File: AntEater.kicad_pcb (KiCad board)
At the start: 4 copper layers, 49.8 x 48.6 mm, 39 parts, among them CN1 X2026WRS-2X09D-LPSW, CN2 X2026WRS-2X09D-LPSW, J2 USB_C_Receptacle_USB2.0, J3 Conn_02x06_Odd_Even, U1 M93C46-WDW6TP, U2 FT4232HQ, U3 RT9080-33GJ5, Y1 12MHz

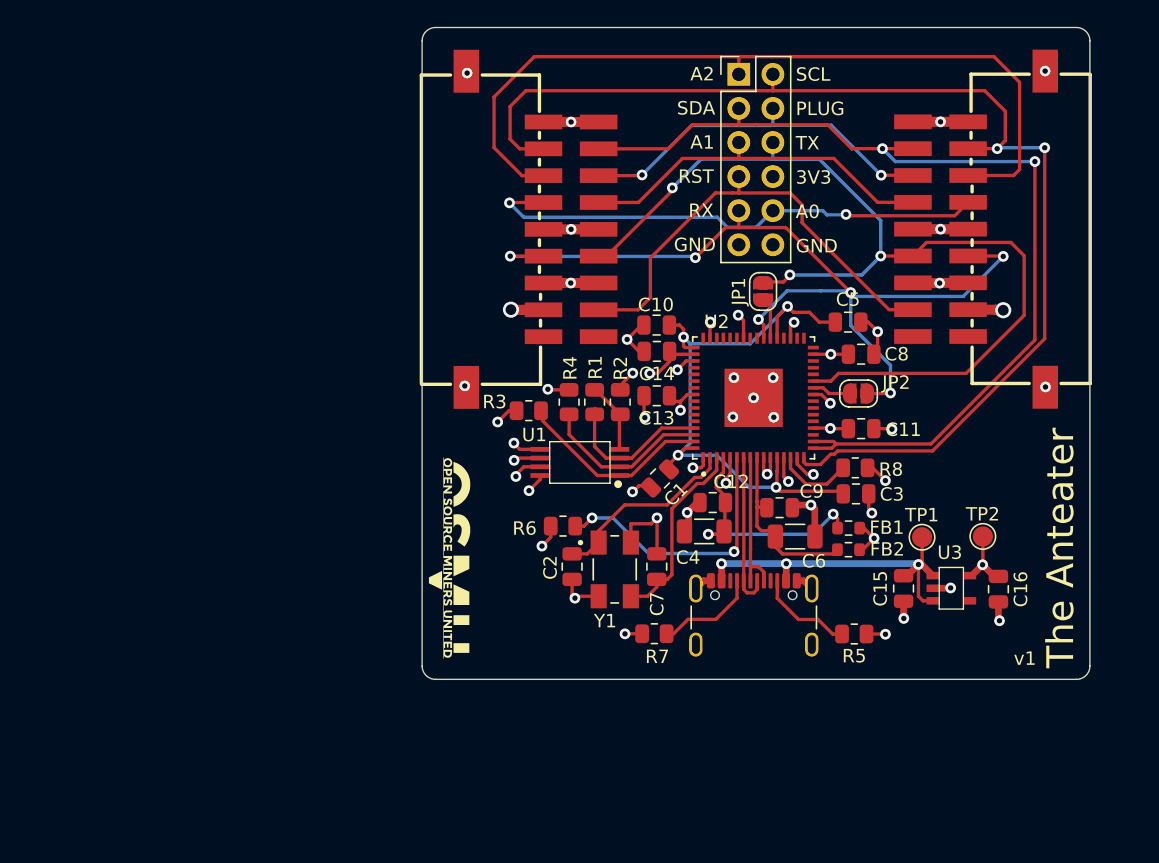
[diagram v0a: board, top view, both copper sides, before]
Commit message: switched schematic to RP2040
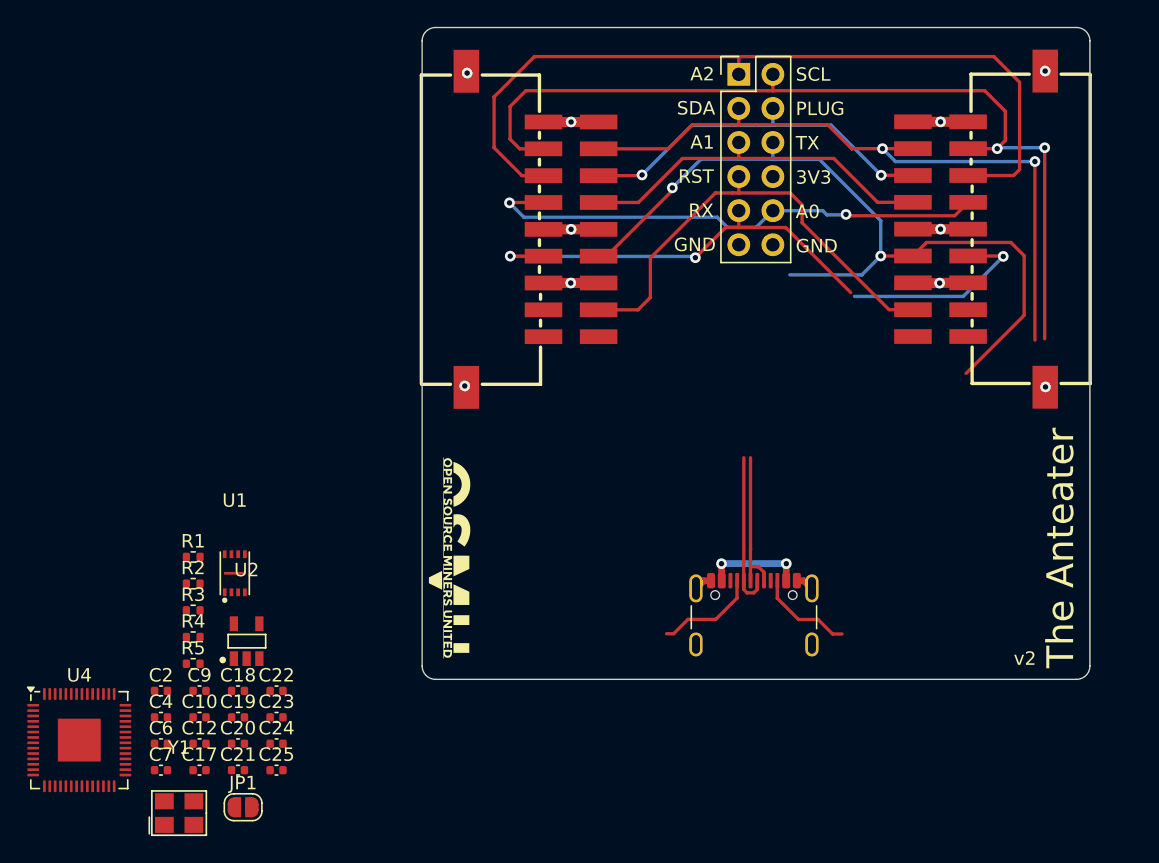
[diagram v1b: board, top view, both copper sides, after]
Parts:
- removed C1, C11, C13, C14, C3, C5, C8: 0.1uF, Capacitor_SMD:C_0805_2012Metric
- removed C15, C16: 1uF, Capacitor_SMD:C_0805_2012Metric
- removed FB1, FB2: FerriteBead_Small, Resistor_SMD:R_0603_1608Metric
- removed J2: USB_C_Receptacle_USB2.0, antsniffer:USB_C_Receptacle_GCT_USB4105-xx-A_16P_TopMnt_Horizontal
- removed JP2: SolderJumper_2_Open, Jumper:SolderJumper-2_P1.3mm_Open_RoundedPad1.0x1.5mm
- removed R6: 12K, Resistor_SMD:R_0805_2012Metric
- removed R7: 5.1K, Resistor_SMD:R_0805_2012Metric
- removed R8: 1K, Resistor_SMD:R_0805_2012Metric
- removed TP1, TP2: TestPoint, TestPoint:TestPoint_Pad_D1.5mm
- removed U3: RT9080-33GJ5, antsniffer:RT9080-33GJ5
- added C17: 1uF, Capacitor_SMD:C_0402_1005Metric, F.Cu at (98.7, 127.7)
- added C18: 1uF, Capacitor_SMD:C_0402_1005Metric, F.Cu at (101.5, 121.8)
- added C19: 0.1uF, Capacitor_SMD:C_0402_1005Metric, F.Cu at (101.5, 123.8)
- added C20: 0.1uF, Capacitor_SMD:C_0402_1005Metric, F.Cu at (101.5, 125.8)
- added C21: 0.1uF, Capacitor_SMD:C_0402_1005Metric, F.Cu at (101.5, 127.7)
- added C22: 0.1uF, Capacitor_SMD:C_0402_1005Metric, F.Cu at (104.4, 121.8)
- added C23: 0.1uF, Capacitor_SMD:C_0402_1005Metric, F.Cu at (104.4, 123.8)
- added C24: 0.1uF, Capacitor_SMD:C_0402_1005Metric, F.Cu at (104.4, 125.8)
- added C25: 0.1uF, Capacitor_SMD:C_0402_1005Metric, F.Cu at (104.4, 127.7)
- added J1: USB_C_Receptacle_USB2.0, antsniffer:USB_C_Receptacle_GCT_USB4105-xx-A_16P_TopMnt_Horizontal, F.Cu at (140.0, 117.3)
- added U4: RP2040, Package_DFN_QFN:QFN-56-1EP_7x7mm_P0.4mm_EP3.2x3.2mm, F.Cu at (89.7, 125.5)
- C10: value 3.3uF -> 0.1uF; footprint Capacitor_SMD:C_0805_2012Metric -> Capacitor_SMD:C_0402_1005Metric
- C12, C9: footprint Capacitor_SMD:C_0805_2012Metric -> Capacitor_SMD:C_0402_1005Metric
- C2, C7: value 27pf -> 1uF; footprint Capacitor_SMD:C_0805_2012Metric -> Capacitor_SMD:C_0402_1005Metric
- C4, C6: value 4.7uF -> 30pF; footprint Capacitor_SMD:C_1206_3216Metric -> Capacitor_SMD:C_0402_1005Metric
- R1: value 2.2K -> 10k; footprint Resistor_SMD:R_0805_2012Metric -> Resistor_SMD:R_0402_1005Metric
- R2, R3: value 10K -> 5.1k; footprint Resistor_SMD:R_0805_2012Metric -> Resistor_SMD:R_0402_1005Metric
- R4: value 10K -> 33; footprint Resistor_SMD:R_0805_2012Metric -> Resistor_SMD:R_0402_1005Metric
- R5: value 5.1K -> 33; footprint Resistor_SMD:R_0805_2012Metric -> Resistor_SMD:R_0402_1005Metric
- U1: value M93C46-WDW6TP -> W25X40CLUXIG TR; footprint bitcrane:TSSOP8_STM -> antsniffer:USON8_L2.0-W3.0-P0.50-BL-EP
- U2: value FT4232HQ -> AP2112K-3.3TRG1; footprint bitcrane:QFN50P900X900X105-65N -> antsniffer:SOT-25-5_L2.9-W1.6-P0.95-LS2.8-BL
- Y1: footprint bitcrane:XTAL_405C35B12M00000 -> antsniffer:OSC-SMD_4P-L3.2-W2.5-BL
- moved JP1 54.6 mm to (101.9, 130.5), turned to 0 degrees
- moved C6 49.7 mm to (95.8, 125.8)
- moved R5 49.3 mm to (98.2, 119.8), turned to 0 degrees
- moved C9 45.3 mm to (98.7, 121.8)
- moved C10 44.9 mm to (98.7, 123.8), turned to 0 degrees
- moved C4 42.8 mm to (95.8, 123.8), turned to 0 degrees
- moved C12 42.3 mm to (98.7, 125.8), turned to 0 degrees
- moved U2 41.9 mm to (102.2, 118.1), turned to 0 degrees
- moved C7 39.9 mm to (95.8, 127.7), turned to 0 degrees
- moved Y1 37.2 mm to (97.2, 130.9)
- moved R2 34.6 mm to (98.2, 113.8), turned to 0 degrees
- moved R4 33.0 mm to (98.2, 117.8), turned to 0 degrees
- moved R1 32.1 mm to (98.2, 111.8), turned to 0 degrees
- moved C2 32.0 mm to (95.8, 121.8), turned to 0 degrees
- moved R3 29.1 mm to (98.2, 115.8), turned to 0 degrees
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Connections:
- C10 pad 1: VCORE -> /GND
- C10 pad 2: /GND -> /1V1
- C12 pad 1: Net-(U2-VPHY) -> /GND
- C12 pad 2: /GND -> /1V1
- C2 pad 1: Net-(U2-OSCI) -> /5V
- C4 pad 1: Net-(U2-VPHY) -> /GND
- C4 pad 2: /GND -> /XOUT
- C6 pad 1: Net-(U2-VPLL) -> /GND
- C6 pad 2: /GND -> /XIN
- C7 pad 1: Net-(U2-OSCO) -> /3V3
- C9 pad 1: Net-(U2-VPLL) -> /GND
- C9 pad 2: /GND -> /3V3
- CN1 pad 15: VCCIO -> /HB_3V3
- CN2 pad 3: VCCIO -> /HB_3V3
- J3 pad 8: VCCIO -> /HB_3V3
- JP1 pad 1: Net-(JP1-A) -> /3V3
- JP1 pad 2: /TX -> /HB_3V3
- R1 pad 1: Net-(U1-D) -> /3V3
- R1 pad 2: Net-(U1-Q) -> /QSPI_SS
- R2 pad 1: Net-(U1-Q) -> /GND
- R2 pad 2: VCCIO -> Net-(J1-CC1)
- R3 pad 1: Net-(U1-CS) -> /GND
- R3 pad 2: VCCIO -> Net-(J1-CC2)
- R4 pad 1: Net-(U1-CLK) -> /USB_DP
- R4 pad 2: VCCIO -> Net-(U4-USB_DP)
- R5 pad 1: /GND -> /USB_DN
- U1 pad 1: Net-(U1-CS) -> /QSPI_SS
- U1 pad 2: Net-(U1-CLK) -> /QSPI_SD1
- U1 pad 3: Net-(U1-D) -> /QSPI_SD2
- U1 pad 4: Net-(U1-Q) -> /GND
- U1 pad 5: /GND -> /QSPI_SD0
- U1 pad 6: VCCIO -> /QSPI_SCLK
- U1 pad 7: /GND -> /QSPI_SD3
- U1 pad 8: VCCIO -> /3V3
- U2 pad 1: /GND -> /5V
- U2 pad 2: Net-(U2-OSCI) -> /GND
- U2 pad 3: Net-(U2-OSCO) -> /5V
- U2 pad 4: Net-(U2-VPHY) -> unconnected-(U2-NC-Pad4)
- U2 pad 5: /GND -> /3V3
- Y1 pad 1: Net-(U2-OSCI) -> /XOUT
- Y1 pad 3: Net-(U2-OSCO) -> /XIN
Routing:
- net /GND: track 84.7 -> 27.7 mm, vias 42 -> 10
- net VCORE: track 46.4 -> 0.00 mm, vias 4 -> 0
- net VCCIO: track 38.5 -> 0.00 mm, vias 15 -> 0
- net /SCL: track 89.7 -> 67.5 mm
- net /SDA: track 72.8 -> 51.2 mm
- net Net-(U2-REF): track 20.3 -> 0.00 mm, vias 2 -> 0
- net /RX: track 67.3 -> 47.0 mm, vias 6 -> 3
- net Net-(U2-VPHY): track 18.6 -> 0.00 mm, vias 2 -> 0
- net /5V: track 25.9 -> 7.39 mm, vias 3 -> 2
- net Net-(U1-CS): track 14.8 -> 0.00 mm
- net Net-(U2-OSCO): track 14.5 -> 0.00 mm
- net Net-(U2-OSCI): track 14.2 -> 0.00 mm
- net /TX: track 73.2 -> 59.3 mm, vias 3 -> 2
- net Net-(U2-VPLL): track 13.5 -> 0.00 mm
- net Net-(U1-CLK): track 12.8 -> 0.00 mm
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- added copper zone on In2.Cu, net /HB_3V3
- removed copper zone on In2.Cu, net VCCIO
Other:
- board text added: "v2"
- board text removed: "v1"

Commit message: switched to RPi Pico
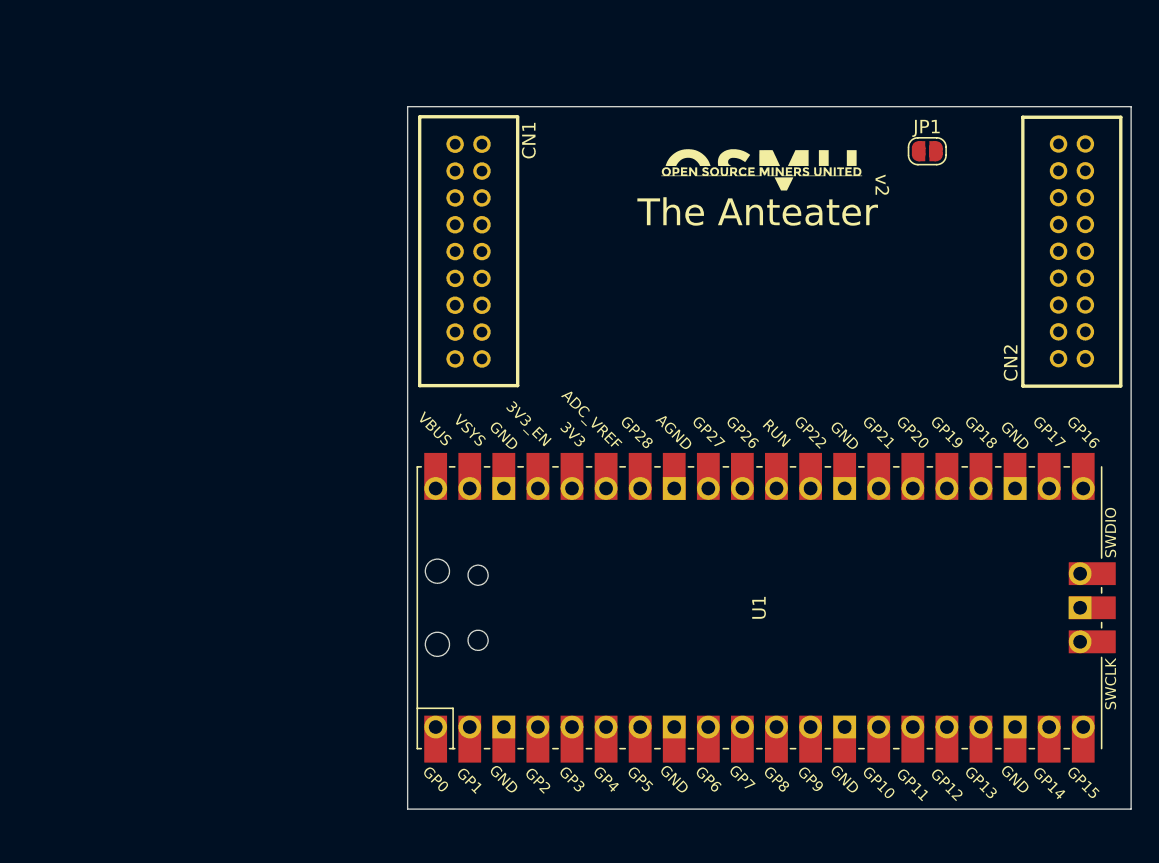
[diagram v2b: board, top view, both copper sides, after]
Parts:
- removed C10, C12, C19, C20, C21, C22, C23, C24, C25, C9: 0.1uF, Capacitor_SMD:C_0402_1005Metric
- removed C17, C18, C2, C7: 1uF, Capacitor_SMD:C_0402_1005Metric
- removed C4, C6: 30pF, Capacitor_SMD:C_0402_1005Metric
- removed J1: USB_C_Receptacle_USB2.0, antsniffer:USB_C_Receptacle_GCT_USB4105-xx-A_16P_TopMnt_Horizontal
- removed J3: Conn_02x06_Odd_Even, Connector_PinHeader_2.54mm:PinHeader_2x06_P2.54mm_Vertical
- removed R1: 10k, Resistor_SMD:R_0402_1005Metric
- removed R2, R3: 5.1k, Resistor_SMD:R_0402_1005Metric
- removed R4, R5: 33, Resistor_SMD:R_0402_1005Metric
- removed U2: AP2112K-3.3TRG1, antsniffer:SOT-25-5_L2.9-W1.6-P0.95-LS2.8-BL
- removed U4: RP2040, Package_DFN_QFN:QFN-56-1EP_7x7mm_P0.4mm_EP3.2x3.2mm
- removed Y1: 12MHz, antsniffer:OSC-SMD_4P-L3.2-W2.5-BL
- CN1, CN2: footprint antsniffer:CONN-SMD_X2026WRS-2X09D-LPSW -> antsniffer:CONN-TH_X2026WV-2-09D-46SN
- U1: value W25X40CLUXIG TR -> Pico; footprint antsniffer:USON8_L2.0-W3.0-P0.50-BL-EP -> antsniffer:RPi_Pico_SMD_TH
- moved JP1 70.6 mm to (152.9, 81.6)
- moved U1 39.2 mm to (140.4, 115.6), turned to 90 degrees
- moved Ge 37.1 mm to (140.6, 83.1), turned to 0 degrees
- moved CN2 7.11 mm to (163.7, 89.1)
- moved CN1 5.03 mm to (118.7, 89.1)
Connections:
- U1 pad 1: /QSPI_SS -> unconnected-(U1-GPIO0-Pad1)
- U1 pad 2: /QSPI_SD1 -> unconnected-(U1-GPIO1-Pad2)
- U1 pad 3: /QSPI_SD2 -> /GND
- U1 pad 4: /GND -> /SDA
- U1 pad 5: /QSPI_SD0 -> /SCL
- U1 pad 6: /QSPI_SCLK -> /RST
- U1 pad 7: /QSPI_SD3 -> /PLUG
- U1 pad 8: /3V3 -> /GND
- U1 pad 9: /GND -> /TX
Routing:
- net /SCL: track 67.5 -> 0.00 mm, vias 2 -> 0
- net /A2: track 61.4 -> 0.00 mm
- net /TX: track 59.3 -> 0.00 mm, vias 2 -> 0
- net /SDA: track 51.2 -> 0.00 mm, vias 2 -> 0
- net /RX: track 47.0 -> 0.00 mm, vias 3 -> 0
- net /A0: track 38.6 -> 0.00 mm, vias 2 -> 0
- net /RST: track 34.4 -> 0.00 mm
- net /PLUG: track 27.8 -> 0.00 mm, vias 2 -> 0
- net /GND: track 27.7 -> 0.00 mm, vias 10 -> 0
- net /A1: track 27.3 -> 0.00 mm
- net /USB_DN: track 11.7 -> 0.00 mm
- net /USB_DP: track 11.0 -> 0.00 mm
- net Net-(J1-CC1): track 7.64 -> 0.00 mm
- net /5V: track 7.39 -> 0.00 mm, vias 2 -> 0
- net Net-(J1-CC2): track 7.23 -> 0.00 mm
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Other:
- board size 49.8 x 48.6 mm -> 53.9 x 52.3 mm
- board text removed: "3V3"
- board text removed: "A0"
- board text removed: "A1"
- board text removed: "A2"
- board text removed: "GND"
- board text removed: "PLUG"
- board text removed: "RST"
- board text removed: "RX"
- board text removed: "SCL"
- board text removed: "SDA"
- board text removed: "TX"
